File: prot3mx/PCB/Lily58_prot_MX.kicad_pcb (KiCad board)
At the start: 2 copper layers, 142.5 x 106.3 mm, 94 parts, among them J1 LED, J2 4PIN, J3 OLED, P1 i2c_pin, P2 i2c_pin, SW1 SW_PUSH, SW10 SW_PUSH, SW11 SW_PUSH, SW12 SW_PUSH, SW13 SW_PUSH, SW14 SW_PUSH, SW15 SW_PUSH, SW16 SW_PUSH, SW17 SW_PUSH, SW18 SW_PUSH, SW19 SW_PUSH, SW2 SW_PUSH, SW20 SW_PUSH, SW21 SW_PUSH, SW22 SW_PUSH, SW23 SW_PUSH, SW24 SW_PUSH, SW25 SW_PUSH, SW26 SW_PUSH, SW27 SW_PUSH, SW28 SW_PUSH, SW29 SW_PUSH, SW3 SW_PUSH, SW30 ROT_ENC_SW, SW31 ROT_ENC_SW, SW32 ROT_ENC_SW, SW4 SW_PUSH, SW5 SW_PUSH, SW6 SW_PUSH, SW7 SW_PUSH, SW8 SW_PUSH, SW9 SW_PUSH, U1 ProMicro

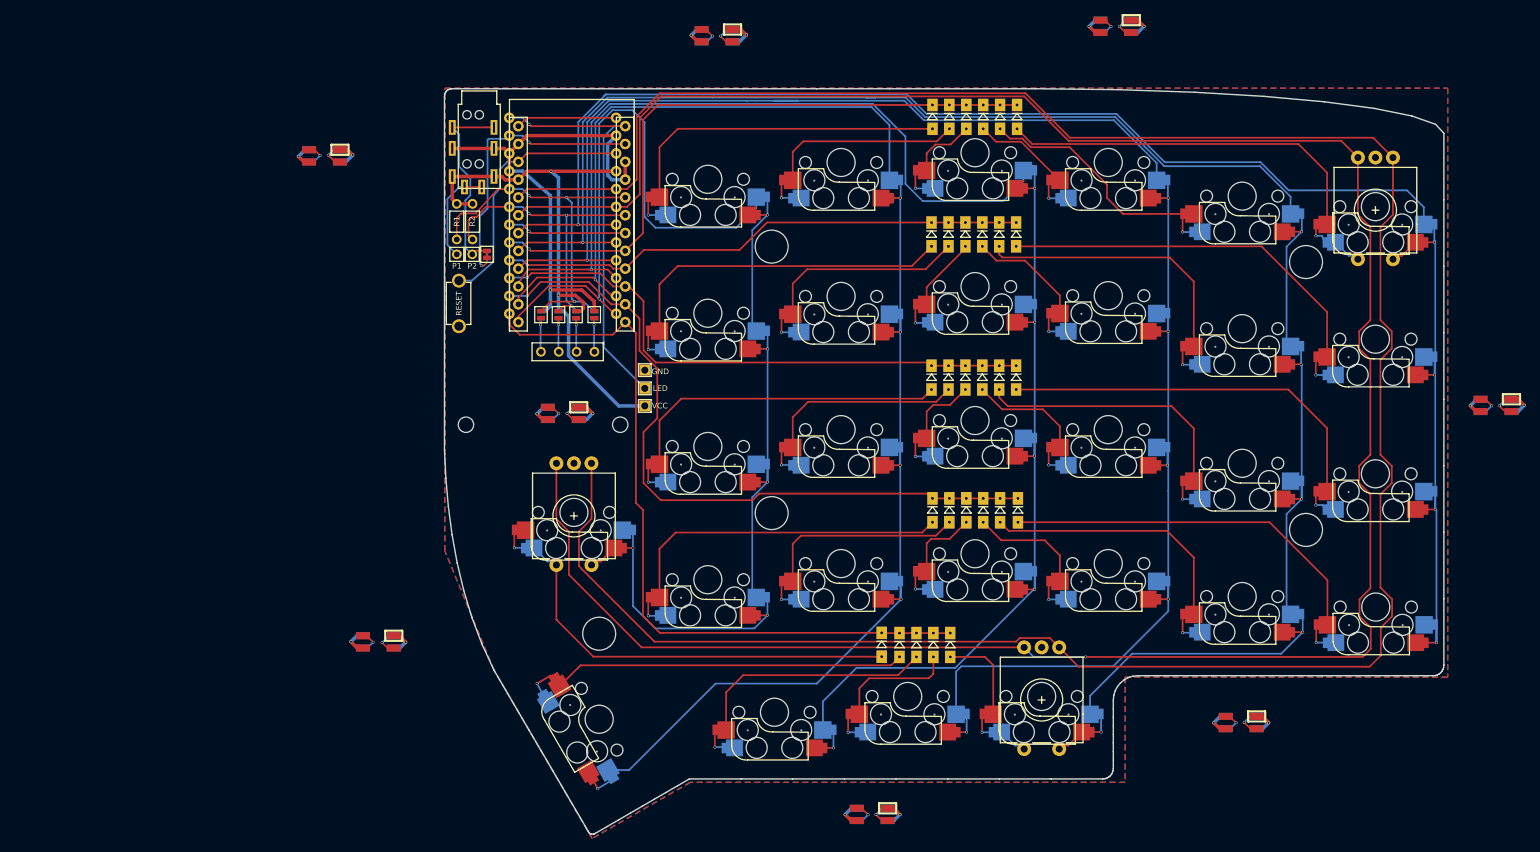
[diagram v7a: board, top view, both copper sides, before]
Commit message: keeping only 1 LED as indicator and fixed all remaining unconnected traces
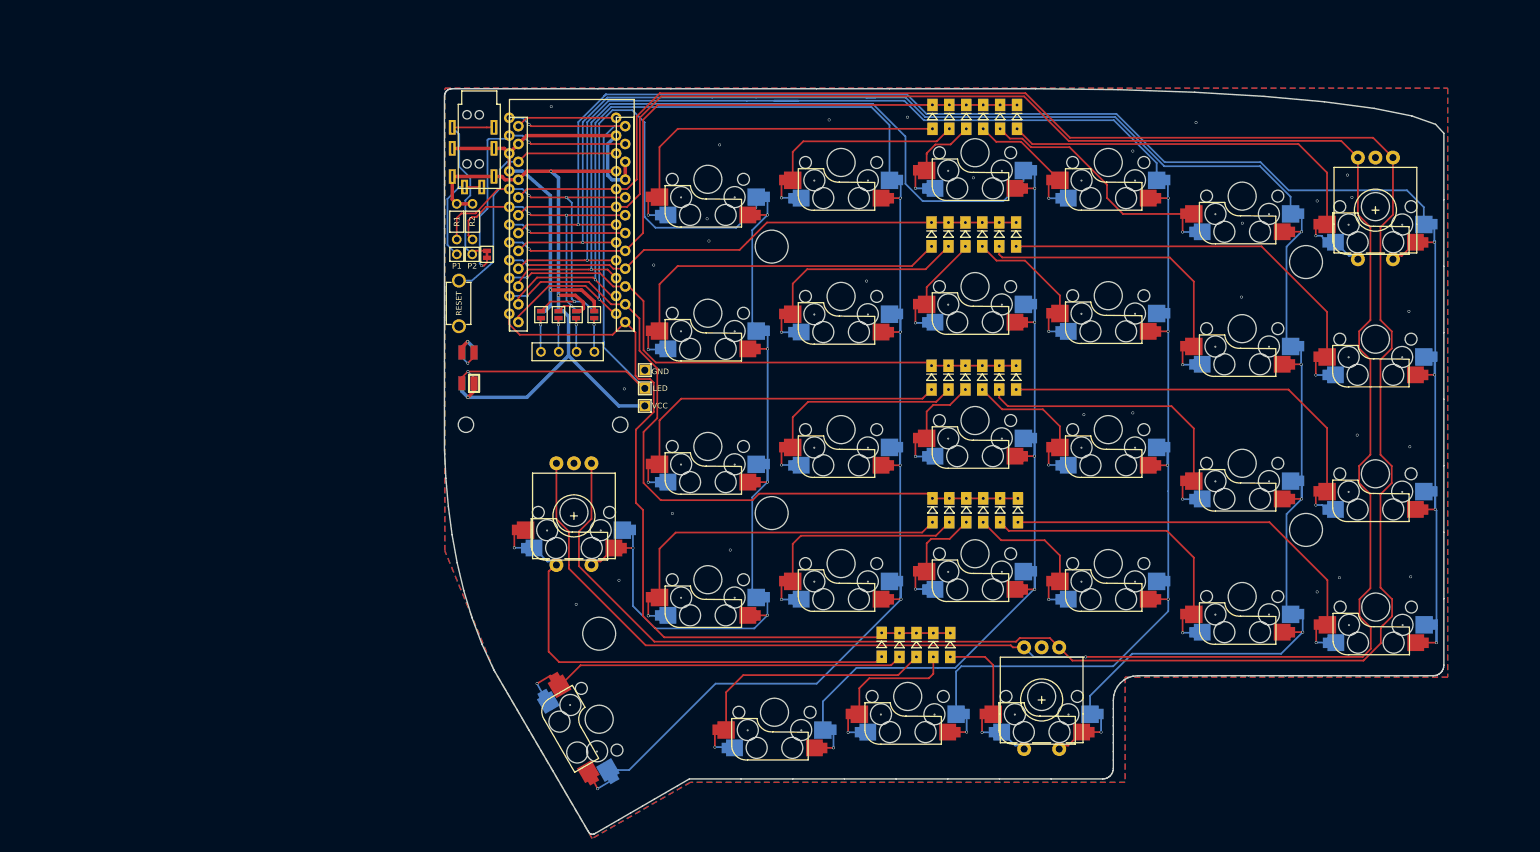
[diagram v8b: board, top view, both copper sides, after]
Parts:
- removed L2, L3, L4, L5, L6, L7, L8: SK6812MINI, Lily58_prot_MX-footprint:SK6812MINI_underglow_rev
- moved L1 15.1 mm to (86.3, 76.9), turned to 270 degrees
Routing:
- net GND: track 102.8 -> 75.4 mm, vias 9 -> 31
- net LED: track 63.6 -> 89.9 mm
- net VCC: track 113.4 -> 99.6 mm, vias 10 -> 3
- net Net-(L4-Pad1): track 8.18 -> 0.00 mm, vias 2 -> 0
- net Net-(L6-Pad1): track 8.03 -> 0.00 mm, vias 2 -> 0
- net Net-(L3-Pad1): track 7.96 -> 0.00 mm, vias 2 -> 0
- net Net-(L2-Pad1): track 7.87 -> 0.00 mm, vias 2 -> 0
- net Net-(L5-Pad1): track 7.75 -> 0.00 mm, vias 2 -> 0
- net Net-(L7-Pad1): track 7.71 -> 0.00 mm, vias 2 -> 0
- net R1_SW1: track 67.4 -> 72.3 mm
- net Net-(L1-Pad1): track 7.99 -> 3.84 mm, vias 2 -> 1
- net Net-(L8-Pad1): track 3.90 -> 0.00 mm, vias 1 -> 0
- net row4: track 107.2 -> 110.8 mm
- net R_A: track 352.5 -> 351.2 mm
- net R_B: track 347.9 -> 347.4 mm
